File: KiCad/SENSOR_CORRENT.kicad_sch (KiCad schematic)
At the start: 5 parts, among them J3 Conn_01x08_Pin, SW3 SW_DPDT_x2

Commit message: V2 placement
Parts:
- C2: footprint (none) -> Capacitor_SMD:C_0805_2012Metric
- R4: footprint (none) -> Resistor_SMD:R_0805_2012Metric
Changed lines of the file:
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@@
 			)
 		)
-		(property "Footprint" ""
+		(property "Footprint" "Resistor_SMD:R_0805_2012Metric"
 			(at 77.978 38.1 90)
 			(effects
@@
 			)
 		)
-		(property "Footprint" ""
+		(property "Footprint" "Capacitor_SMD:C_0805_2012Metric"
 			(at 56.8452 50.8 0)
 			(effects

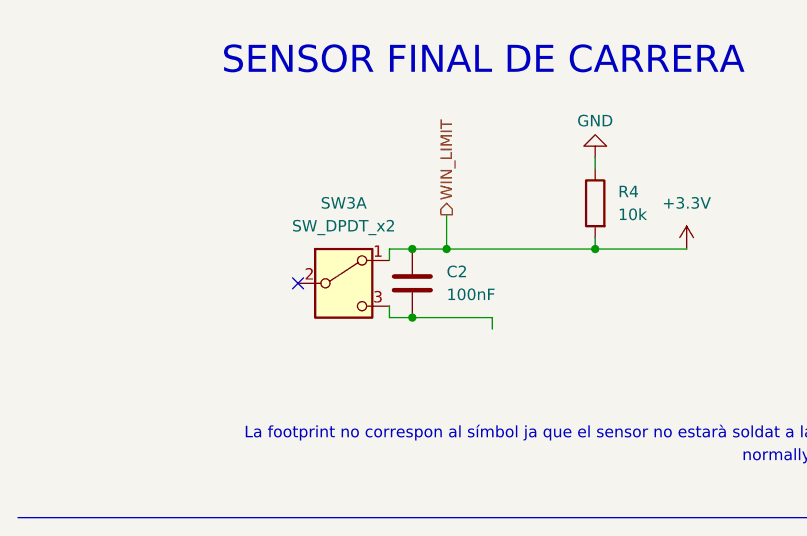
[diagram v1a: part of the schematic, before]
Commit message: REORDENACIÓ DEL MICRO
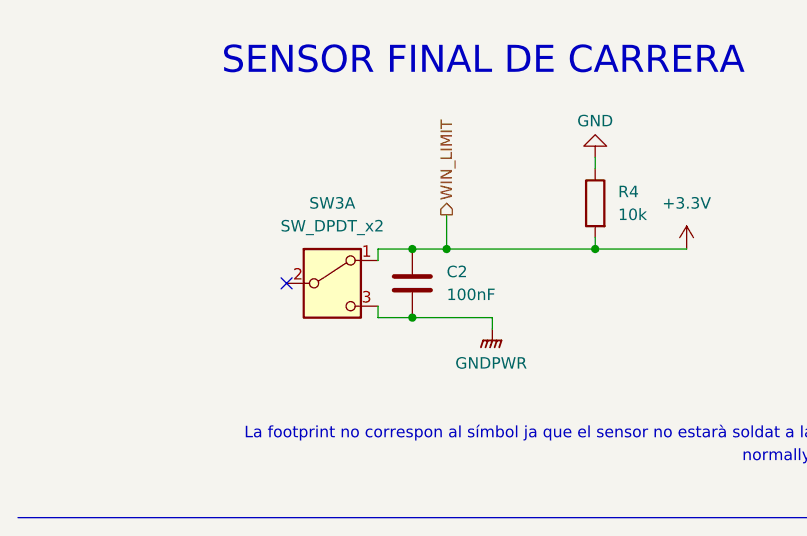
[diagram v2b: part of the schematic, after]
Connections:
- net GNDPWR: now reaches C2.2, SW3.3 (C)
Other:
- moved on the sheet: SW3A
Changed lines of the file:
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@@
 	)
 	(no_connect
-		(at 43.18 46.99)
+		(at 41.91 46.99)
 	)
 	(polyline
@@
 	(wire
 		(pts
-			(xy 53.34 43.18) (xy 55.88 43.18)
+			(xy 52.07 43.18) (xy 55.88 43.18)
 		)
 		(stroke
@@
 	(wire
 		(pts
-			(xy 53.34 50.8) (xy 55.88 50.8)
+			(xy 52.07 50.8) (xy 55.88 50.8)
 		)
 		(stroke
@@
 	(wire
 		(pts
-			(xy 53.34 50.8) (xy 53.34 49.53)
+			(xy 52.07 50.8) (xy 52.07 49.53)
 		)
 		(stroke
@@
 	(wire
 		(pts
-			(xy 53.34 43.18) (xy 53.34 44.45)
+			(xy 52.07 43.18) (xy 52.07 44.45)
 		)
 		(stroke
@@
 	(symbol
 		(lib_id "Switch:SW_DPDT_x2")
-		(at 48.26 46.99 0)
+		(at 46.99 46.99 0)
 		(unit 1)
 		(exclude_from_sim no)
@@
 		(fields_autoplaced yes)
 		(property "Reference" "SW3"
-			(at 48.26 38.1 0)
+			(at 46.99 38.1 0)
 			(effects
 				(font
@@
 		)
 		(property "Value" "SW_DPDT_x2"
-			(at 48.26 40.64 0)
+			(at 46.99 40.64 0)
 			(effects
 				(font
@@
 		)
 		(property "Footprint" "Button_Switch_SMD:SW_DPDT_CK_JS202011JCQN"
-			(at 48.26 46.99 0)
+			(at 46.99 46.99 0)
 			(effects
 				(font
@@
 		)
 		(property "Datasheet" "~"
-			(at 48.26 46.99 0)
+			(at 46.99 46.99 0)
 			(effects
 				(font
@@
 		)
 		(property "Description" "Switch, dual pole double throw, separate symbols"
-			(at 48.26 46.99 0)
+			(at 46.99 46.99 0)
 			(effects
 				(font
@@
 					(unit 1)
 				)
+			)
+		)
+	)
+	(symbol
+		(lib_id "power:GNDPWR")
+		(at 64.77 52.07 0)
+		(unit 1)
+		(exclude_from_sim no)
+		(in_bom yes)
+		(on_board yes)
+		(dnp no)
+		(fields_autoplaced yes)
+		(property "Reference" "#PWR021"
+			(at 64.77 57.15 0)
+			(effects
+				(font
+					(size 1.27 1.27)
+				)
+				(hide yes)
+			)
+		)
+		(property "Value" "GNDPWR"
+			(at 64.643 55.88 0)
+			(effects
+				(font
+					(size 1.27 1.27)
+				)
+			)
+		)
+		(property "Footprint" ""
+			(at 64.77 53.34 0)
+			(effects
+				(font
+					(size 1.27 1.27)
+				)
+				(hide yes)
+			)
+		)
+		(property "Datasheet" ""
+			(at 64.77 53.34 0)
+			(effects
+				(font
+					(size 1.27 1.27)
+				)
+				(hide yes)
+			)
+		)
+		(property "Description" "Power symbol creates a global label with name \"GNDPWR\" , global ground"
+			(at 64.77 52.07 0)
+			(effects
+				(font
+					(size 1.27 1.27)
+				)
+				(hide yes)
+			)
+		)
+		(pin "1"
+		)
+		(instances
+			(project ""
+				(path "/347831db-5db9-4aff-ad32-e56fd770e219/0aa311db-868d-4102-819d-96f0255ccb92"
+					(reference "#PWR021")
+					(unit 1)
+				)

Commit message: V1 Routing
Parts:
- C2: footprint Capacitor_SMD:C_0805_2012Metric -> (none)
- R4: footprint Resistor_SMD:R_0805_2012Metric -> (none)
- SW3: footprint Button_Switch_SMD:SW_DPDT_CK_JS202011JCQN -> TerminalBlock:TerminalBlock_MaiXu_MX126-5.0-02P_1x02_P5.00mm
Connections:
- net GNDPWR is gone; now on net GND: C2.2, SW3.3 (C)
- net RFID_CS: now also J3.3 (MOSI); no longer J3.1 (SDA)
- net RFID_MISO: now also J3.2 (SCK); no longer J3.4 (MISO)
- net RFID_MOSI: now also J3.1 (SDA); no longer J3.3 (MOSI)
- net RFID_RST: now also J3.4 (MISO); no longer J3.5 (IRQ)
- net RFID_SCK: now also J3.5 (IRQ); no longer J3.2 (SCK)
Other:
- note removed: "normally open"
- moved on the sheet: SW3A
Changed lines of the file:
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@@
 	(text "La footprint no correspon al símbol ja que el sensor no estarà soldat a la PCB."
 		(exclude_from_sim no)
-		(at 71.12 63.754 0)
+		(at 61.468 60.706 0)
 		(effects
 			(font
@@
 	(text "serial clock"
 		(exclude_from_sim no)
-		(at 159.766 55.88 0)
+		(at 160.274 48.26 0)
 		(effects
 			(font
@@
 	(text "slave select"
 		(exclude_from_sim no)
-		(at 160.02 58.42 0)
+		(at 160.528 53.34 0)
 		(effects
 			(font
@@
 		)
 	)
-	(text "normally open"
-		(exclude_from_sim no)
-		(at 98.806 66.294 0)
-		(effects
-			(font
-				(size 1.27 1.27)
-			)
-		)
-	)
 	(text "master in"
 		(exclude_from_sim no)
-		(at 159.004 50.8 0)
+		(at 159.258 55.88 0)
 		(effects
 			(font
@@
 	(text "reset"
 		(exclude_from_sim no)
-		(at 156.972 48.26 0)
+		(at 156.972 51.054 0)
 		(effects
 			(font
@@
 	(text "master out"
 		(exclude_from_sim no)
-		(at 159.512 53.34 0)
+		(at 159.766 58.42 0)
 		(effects
 			(font
@@
 	)
 	(no_connect
-		(at 41.91 46.99)
+		(at 43.18 46.99)
 	)
 	(polyline
@@
 	(wire
 		(pts
-			(xy 52.07 43.18) (xy 55.88 43.18)
+			(xy 53.34 43.18) (xy 55.88 43.18)
 		)
 		(stroke
@@
 	(wire
 		(pts
-			(xy 52.07 50.8) (xy 55.88 50.8)
+			(xy 53.34 50.8) (xy 55.88 50.8)
 		)
 		(stroke
@@
 	(wire
 		(pts
+			(xy 147.32 53.34) (xy 148.59 53.34)
+		)
+		(stroke
+			(width 0)
+			(type default)
+		)
+	)
+	(wire
+		(pts
 			(xy 76.2 43.18) (xy 86.36 43.18)
 		)
@@
 	(wire
 		(pts
-			(xy 52.07 50.8) (xy 52.07 49.53)
+			(xy 53.34 50.8) (xy 53.34 49.53)
 		)
 		(stroke
@@
 	(wire
 		(pts
-			(xy 52.07 43.18) (xy 52.07 44.45)
+			(xy 53.34 43.18) (xy 53.34 44.45)
 		)
 		(stroke
@@
 	(hierarchical_label "RFID_RST"
 		(shape input)
-		(at 148.59 48.26 180)
+		(at 144.78 50.8 180)
 		(effects
 			(font
@@
 	(hierarchical_label "RFID_MOSI"
 		(shape input)
-		(at 148.59 53.34 180)
+		(at 148.59 58.42 180)
 		(effects
 			(font
@@
 	(hierarchical_label "RFID_MISO"
 		(shape output)
-		(at 144.78 50.8 180)
+		(at 144.78 55.88 180)
 		(effects
 			(font
@@
 	(hierarchical_label "RFID_SCK"
 		(shape input)
-		(at 144.78 55.88 180)
+		(at 148.59 48.26 180)
 		(effects
 			(font
@@
 	(hierarchical_label "RFID_CS"
 		(shape input)
-		(at 148.59 58.42 180)
+		(at 147.32 53.34 180)
 		(effects
 			(font
@@
 		(dnp no)
 		(fields_autoplaced yes)
-		(property "Reference" "#PWR049"
+		(property "Reference" "#PWR046"
 			(at 86.36 46.99 0)
 			(effects
@@
 			(project ""
 				(path "/347831db-5db9-4aff-ad32-e56fd770e219/0aa311db-868d-4102-819d-96f0255ccb92"
-					(reference "#PWR049")
+					(reference "#PWR046")
 					(unit 1)
 				)
@@
 		(on_board yes)
 		(dnp no)
-		(property "Reference" "#PWR047"
+		(property "Reference" "#PWR048"
 			(at 134.62 49.53 0)
 			(effects
@@
 			(project "PROJECTE_EINES"
 				(path "/347831db-5db9-4aff-ad32-e56fd770e219/0aa311db-868d-4102-819d-96f0255ccb92"
-					(reference "#PWR047")
+					(reference "#PWR048")
 					(unit 1)
 				)
@@
 			)
 		)
-		(property "Footprint" "Resistor_SMD:R_0805_2012Metric"
+		(property "Footprint" ""
 			(at 77.978 38.1 90)
 			(effects
@@
 	(symbol
 		(lib_id "power:GND")
+		(at 64.77 52.07 0)
+		(unit 1)
+		(exclude_from_sim no)
+		(in_bom yes)
+		(on_board yes)
+		(dnp no)
+		(fields_autoplaced yes)
+		(property "Reference" "#PWR044"
+			(at 64.77 58.42 0)
+			(effects
+				(font
+					(size 1.27 1.27)
+				)
+				(hide yes)
+			)
+		)
+		(property "Value" "GND"
+			(at 64.77 57.15 0)
+			(effects
+				(font
+					(size 1.27 1.27)
+				)
+			)
+		)
+		(property "Footprint" ""
+			(at 64.77 52.07 0)
+			(effects
+				(font
+					(size 1.27 1.27)
+				)
+				(hide yes)
+			)
+		)
+		(property "Datasheet" ""
+			(at 64.77 52.07 0)
+			(effects
+				(font
+					(size 1.27 1.27)
+				)
+				(hide yes)
+			)
+		)
+		(property "Description" "Power symbol creates a global label with name \"GND\" , ground"
+			(at 64.77 52.07 0)
+			(effects
+				(font
+					(size 1.27 1.27)
+				)
+				(hide yes)
+			)
+		)
+		(pin "1"
+		)
+		(instances
+			(project ""
+				(path "/347831db-5db9-4aff-ad32-e56fd770e219/0aa311db-868d-4102-819d-96f0255ccb92"
+					(reference "#PWR044")
+					(unit 1)
+				)
+			)
+		)
+	)
+	(symbol
+		(lib_id "power:GND")
 		(at 134.62 40.64 180)
 		(unit 1)
@@
 		(dnp no)
 		(fields_autoplaced yes)
-		(property "Reference" "#PWR046"
+		(property "Reference" "#PWR047"
 			(at 134.62 34.29 0)
 			(effects
@@
 			(project "PROJECTE_EINES"
 				(path "/347831db-5db9-4aff-ad32-e56fd770e219/0aa311db-868d-4102-819d-96f0255ccb92"
-					(reference "#PWR046")
+					(reference "#PWR047")
 					(unit 1)
 				)
@@
 	(symbol
 		(lib_id "Switch:SW_DPDT_x2")
-		(at 46.99 46.99 0)
+		(at 48.26 46.99 0)
 		(unit 1)
 		(exclude_from_sim no)
@@
 		(fields_autoplaced yes)
 		(property "Reference" "SW3"
-			(at 46.99 38.1 0)
+			(at 48.26 38.1 0)
 			(effects
 				(font
@@
 		)
 		(property "Value" "SW_DPDT_x2"
-			(at 46.99 40.64 0)
+			(at 48.26 40.64 0)
 			(effects
 				(font
@@
 			)
 		)
-		(property "Footprint" "Button_Switch_SMD:SW_DPDT_CK_JS202011JCQN"
-			(at 46.99 46.99 0)
+		(property "Footprint" "TerminalBlock:TerminalBlock_MaiXu_MX126-5.0-02P_1x02_P5.00mm"
+			(at 48.26 46.99 0)
 			(effects
 				(font
@@
 		)
 		(property "Datasheet" "~"
-			(at 46.99 46.99 0)
+			(at 48.26 46.99 0)
 			(effects
 				(font
@@
 		)
 		(property "Description" "Switch, dual pole double throw, separate symbols"
-			(at 46.99 46.99 0)
+			(at 48.26 46.99 0)
 			(effects
 				(font
@@
 			)
 		)
-		(property "Footprint" "Capacitor_SMD:C_0805_2012Metric"
+		(property "Footprint" ""
 			(at 56.8452 50.8 0)
 			(effects
@@
 					(unit 1)
 				)
-			)
-		)
-	)
-	(symbol
-		(lib_id "power:GNDPWR")
-		(at 64.77 52.07 0)
-		(unit 1)
-		(exclude_from_sim no)
-		(in_bom yes)
-		(on_board yes)
-		(dnp no)
-		(fields_autoplaced yes)
-		(property "Reference" "#PWR021"
-			(at 64.77 57.15 0)
-			(effects
-				(font
-					(size 1.27 1.27)
-				)
-				(hide yes)
-			)
-		)
-		(property "Value" "GNDPWR"
-			(at 64.643 55.88 0)
-			(effects
-				(font
-					(size 1.27 1.27)
-				)
-			)
-		)
-		(property "Footprint" ""
-			(at 64.77 53.34 0)
-			(effects
-				(font
-					(size 1.27 1.27)
-				)
-				(hide yes)
-			)
-		)
-		(property "Datasheet" ""
-			(at 64.77 53.34 0)
-			(effects
-				(font
-					(size 1.27 1.27)
-				)
-				(hide yes)
-			)
-		)
-		(property "Description" "Power symbol creates a global label with name \"GNDPWR\" , global ground"
-			(at 64.77 52.07 0)
-			(effects
-				(font
-					(size 1.27 1.27)
-				)
-				(hide yes)
-			)
-		)
-		(pin "1"
-		)
-		(instances
-			(project ""
-				(path "/347831db-5db9-4aff-ad32-e56fd770e219/0aa311db-868d-4102-819d-96f0255ccb92"
-					(reference "#PWR021")
-					(unit 1)
-				)

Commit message: Actualització dels test points
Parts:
- C2: footprint (none) -> Capacitor_SMD:C_0805_2012Metric
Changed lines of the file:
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@@
 			)
 		)
-		(property "Footprint" ""
+		(property "Footprint" "Capacitor_SMD:C_0805_2012Metric"
 			(at 56.8452 50.8 0)
 			(effects

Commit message: Versio final KiCad, BOM i Diagrama de Blocs
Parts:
- C2: value 100nF -> 100n
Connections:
- net +3.3V: now also R4.1; no longer C2.1, R4.2, SW3.1 (A)
- net GND: now also C2.1, SW3.2 (B); no longer C2.2, R4.1, SW3.3 (C)
- new net WIN_LIMIT: C2.2, R4.2, SW3.1 (A)
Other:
- note added: "COM"
- note added: "Decoupling capacitor"
- note added: "NC"
- note added: "NO"
- note added: "REFERENCIA DE COM ES VEU UN SENSOR AL QUAL CONECTAREM A LA PCB És una peça externa a la PCB, anirà conectada amb cables a partir del conector."
- note added: "Sensor final de carrera a utilitzar"
- note removed: "REFERENCIA DE COM ES VEU UN SENSOR AL QUAL CONECTAREM A LA PCB"
- note removed: "decoupling capacitor"
- moved on the sheet: R4, SW3A

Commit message: Afegida foodprint a R4 i actualitzada a la PCB
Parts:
- R4: footprint (none) -> Resistor_SMD:R_0805_2012Metric
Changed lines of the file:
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@@
 			)
 		)
-		(property "Footprint" ""
+		(property "Footprint" "Resistor_SMD:R_0805_2012Metric"
 			(at 66.548 41.91 90)
 			(effects

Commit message: Versió Final projecte
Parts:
- renumbered C2 to C21, C3 to C22, R4 to R13
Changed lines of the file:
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@@
 		(dnp no)
 		(fields_autoplaced yes)
-		(property "Reference" "#PWR046"
+		(property "Reference" "#PWR045"
 			(at 64.77 40.64 0)
 			(effects
@@
 			(project ""
 				(path "/347831db-5db9-4aff-ad32-e56fd770e219/0aa311db-868d-4102-819d-96f0255ccb92"
-					(reference "#PWR046")
+					(reference "#PWR045")
 					(unit 1)
 				)
@@
 		(on_board yes)
 		(dnp no)
-		(property "Reference" "#PWR045"
+		(property "Reference" "#PWR044"
 			(at 31.75 57.15 0)
 			(effects
@@
 			(project "PROJECTE_EINES"
 				(path "/347831db-5db9-4aff-ad32-e56fd770e219/0aa311db-868d-4102-819d-96f0255ccb92"
-					(reference "#PWR045")
+					(reference "#PWR044")
 					(unit 1)
 				)
@@
 		(on_board yes)
 		(dnp no)
-		(property "Reference" "#PWR048"
+		(property "Reference" "#PWR047"
 			(at 134.62 49.53 0)
 			(effects
@@
 			(project "PROJECTE_EINES"
 				(path "/347831db-5db9-4aff-ad32-e56fd770e219/0aa311db-868d-4102-819d-96f0255ccb92"
-					(reference "#PWR048")
+					(reference "#PWR047")
 					(unit 1)
 				)
@@
 		(dnp no)
 		(fields_autoplaced yes)
-		(property "Reference" "R4"
+		(property "Reference" "R13"
 			(at 67.31 40.6399 0)
 			(effects
@@
 			(project "PROJECTE_EINES"
 				(path "/347831db-5db9-4aff-ad32-e56fd770e219/0aa311db-868d-4102-819d-96f0255ccb92"
-					(reference "R4")
+					(reference "R13")
 					(unit 1)
 				)
@@
 		(dnp no)
 		(fields_autoplaced yes)
-		(property "Reference" "#PWR047"
+		(property "Reference" "#PWR046"
 			(at 134.62 34.29 0)
 			(effects
@@
 			(project "PROJECTE_EINES"
 				(path "/347831db-5db9-4aff-ad32-e56fd770e219/0aa311db-868d-4102-819d-96f0255ccb92"
-					(reference "#PWR047")
+					(reference "#PWR046")
 					(unit 1)
 				)
@@
 		(on_board yes)
 		(dnp no)
-		(property "Reference" "C3"
+		(property "Reference" "C22"
 			(at 143.51 36.83 90)
 			(effects
@@
 			(project "PROJECTE_EINES"
 				(path "/347831db-5db9-4aff-ad32-e56fd770e219/0aa311db-868d-4102-819d-96f0255ccb92"
-					(reference "C3")
+					(reference "C22")
 					(unit 1)
 				)
@@
 		(dnp no)
 		(fields_autoplaced yes)
-		(property "Reference" "C2"
+		(property "Reference" "C21"
 			(at 45.72 27.94 90)
 			(effects
@@
 			(project ""
 				(path "/347831db-5db9-4aff-ad32-e56fd770e219/0aa311db-868d-4102-819d-96f0255ccb92"
-					(reference "C2")
-					(unit 1)
-				)
+					(reference "C21")
+					(unit 1)
+				)
